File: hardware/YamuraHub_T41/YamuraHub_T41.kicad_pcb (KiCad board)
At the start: 2 copper layers, 120 x 80 mm, 29 parts, among them J1 12V in, J2 CAN H/L (from A3), J3 DB9 male - CAN bus, J4 Display (MSP4030/4031 14-pin), J5 I2C (Wire2) / GPS, J6 Panel buttons, J7 Panel LEDs, SW1 SELECT, SW2 UP, SW3 DOWN, U1 R-78E5.0-1.0

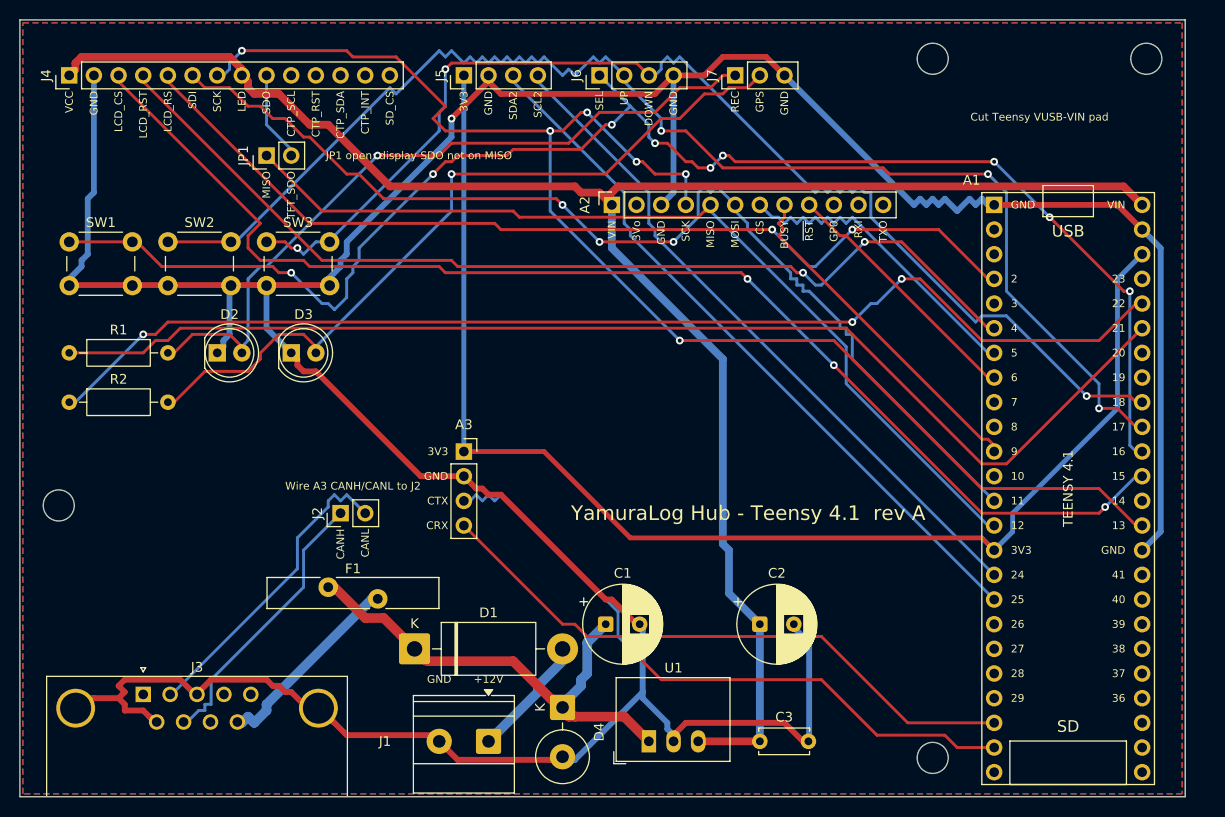
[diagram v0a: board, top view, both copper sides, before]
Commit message: Hub carrier board rev B: display on front, parts on back, two DB9s
- 122 x 68 mm board: the 4" display (MSP4030/4031) plugs into J4 on the
  front, long side along the board, on M3 standoffs at its own holes
  (H5-H8); every other part is on the back; M3 holes at the corners.
- Second DB9 (J8) in parallel with J3 so the CAN bus can pass through
  the hub. Waveshare terminator must come off if both are used.
- Buttons and LEDs are panel-mounted: SW1-3 and D2/D3 removed, J6/J7
  headers kept (R1/R2 still on board).
- build_pcb.py flips side "B" parts to the back with mirrored back-side
  silkscreen and draws the display outline on the front.
- route.py rips up and retries with failed nets first; pad stubs only
  from real track endpoints.
- Fab outputs, BOM, renders and README regenerated for rev B.

ERC clean; DRC with schematic parity: 0 unconnected, 0 mismatches,
no courtyard/clearance errors (two starved-thermal warnings only).

Co-Authored-By: Claude Opus 5.5 <noreply@anthropic.com>
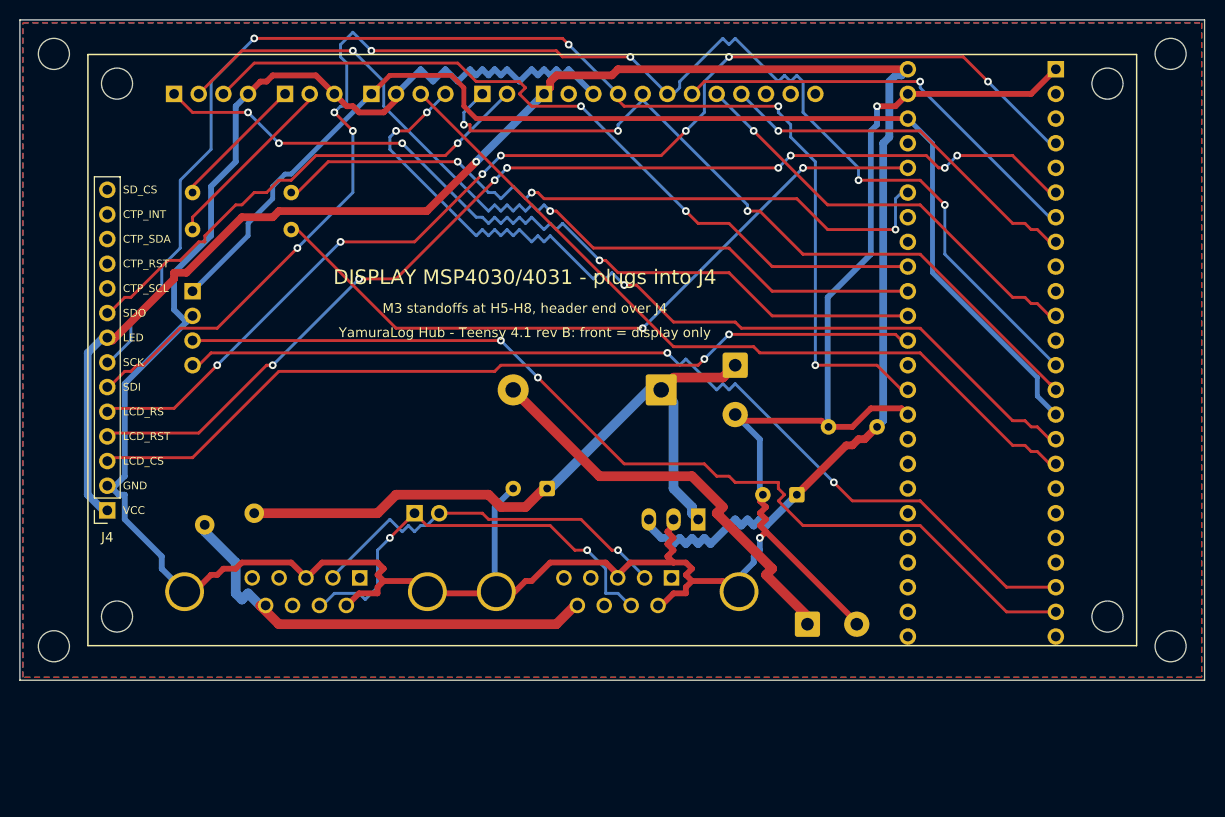
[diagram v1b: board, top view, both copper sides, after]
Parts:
- removed D2: Red (REC), LED_THT:LED_D5.0mm
- removed D3: Green (GPS), LED_THT:LED_D5.0mm
- removed SW1: SELECT, Button_Switch_THT:SW_PUSH_6mm
- removed SW2: UP, Button_Switch_THT:SW_PUSH_6mm
- removed SW3: DOWN, Button_Switch_THT:SW_PUSH_6mm
- added H5: M3 (display), MountingHole:MountingHole_3.2mm_M3, F.Cu at (10.0, 6.56)
- added H6: M3 (display), MountingHole:MountingHole_3.2mm_M3, F.Cu at (112.0, 6.56)
- added H7: M3 (display), MountingHole:MountingHole_3.2mm_M3, F.Cu at (10.0, 61.4)
- added H8: M3 (display), MountingHole:MountingHole_3.2mm_M3, F.Cu at (112.0, 61.4)
- added J8: DB9 male - CAN bus 2, Connector_Dsub:DSUB-9_Pins_Horizontal_P2.77x2.84mm_EdgePinOffset7.70mm_Housed_MountingHolesOffset9.12mm, B.Cu at (67.1, 57.5)
- A1, A2, A3, C1, C2, C3, D1, D4, F1, J1, J2, J5, J6, J7, JP1, R1, R2, U1: moved to B.Cu
- H1, H2, H3, H4: value M3 -> M3 (board)
- J3: value DB9 male - CAN bus -> DB9 male - CAN bus 1; moved to B.Cu
- J4: value Display (MSP4030/4031 14-pin) -> Display socket (MSP4030/4031 14-pin); footprint Connector_PinHeader_2.54mm:PinHeader_1x14_P2.54mm_Vertical -> Connector_PinSocket_2.54mm:PinSocket_1x14_P2.54mm_Vertical
- moved H3 91.2 mm to (3.50, 64.5)
- moved H4 60.6 mm to (118.5, 64.5)
- moved H1 46.5 mm to (3.50, 3.50)
- moved J7 46.4 mm to (27.3, 7.62), turned to -90 degrees
- moved J4 45.0 mm to (9.00, 50.5), turned to 180 degrees
- moved J6 43.9 mm to (15.9, 7.62), turned to -90 degrees
- moved D4 39.5 mm to (73.7, 35.6)
- moved D1 36.8 mm to (66.0, 38.1), turned to 180 degrees
- moved J1 35.0 mm to (81.1, 62.2), turned to 0 degrees
- moved C3 34.6 mm to (88.3, 41.9), turned to 180 degrees
- moved A3 32.5 mm to (17.8, 27.9), turned to 180 degrees
- moved R2 29.0 mm to (27.9, 21.6), turned to 180 degrees
- moved R1 28.2 mm to (27.9, 17.8), turned to 180 degrees
- moved J3 25.3 mm to (35.0, 57.5), turned to 180 degrees
- moved H2 24.5 mm to (118.5, 3.50)
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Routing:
- net GND: track 396.3 -> 310.1 mm, vias 1 -> 2
- net BTN_SELECT: track 153.3 -> 87.6 mm, vias 9 -> 4
- net LED_REC: track 74.4 -> 13.5 mm, vias 1 -> 0
- net LED_GPS: track 77.7 -> 17.7 mm, vias 1 -> 0
- net LED_REC_DRV: track 122.5 -> 71.5 mm, vias 0 -> 3
- net BTN_UP: track 138.5 -> 88.6 mm, vias 3 -> 2
- net LED_GPS_DRV: track 118.7 -> 73.3 mm, vias 3 -> 2
- net TFT_MISO: track 8.04 -> 50.8 mm, vias 0 -> 1
- net TFT_CS: track 128.0 -> 87.4 mm, vias 3 -> 2
- net BTN_DOWN: track 121.4 -> 81.1 mm, vias 3 -> 2
- net MOSI: track 110.6 -> 150.8 mm, vias 3 -> 7
- net CAN_RX: track 62.4 -> 99.7 mm, vias 0 -> 2
- net CAN_TX: track 66.9 -> 100.8 mm, vias 1 -> 2
- net +12V_IN: track 10.5 -> 42.5 mm
- net +12V_BUS: track 20.6 -> 47.3 mm
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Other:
- board size 120 x 80 mm -> 122 x 68 mm
- board text added: "DISPLAY MSP4030/4031 - plugs into J4"
- board text added: "M3 standoffs at H5-H8, header end over J4"
- board text added: "YamuraLog Hub - Teensy 4.1 rev B"
- board text added: "YamuraLog Hub - Teensy 4.1 rev B: front = display only"
- board text removed: "YamuraLog Hub - Teensy 4.1 rev A"
